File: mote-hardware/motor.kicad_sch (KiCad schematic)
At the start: 16 parts, among them J7 JST_PH_B6B, J8 JST_PH_B6B, U5 DRV8833PW

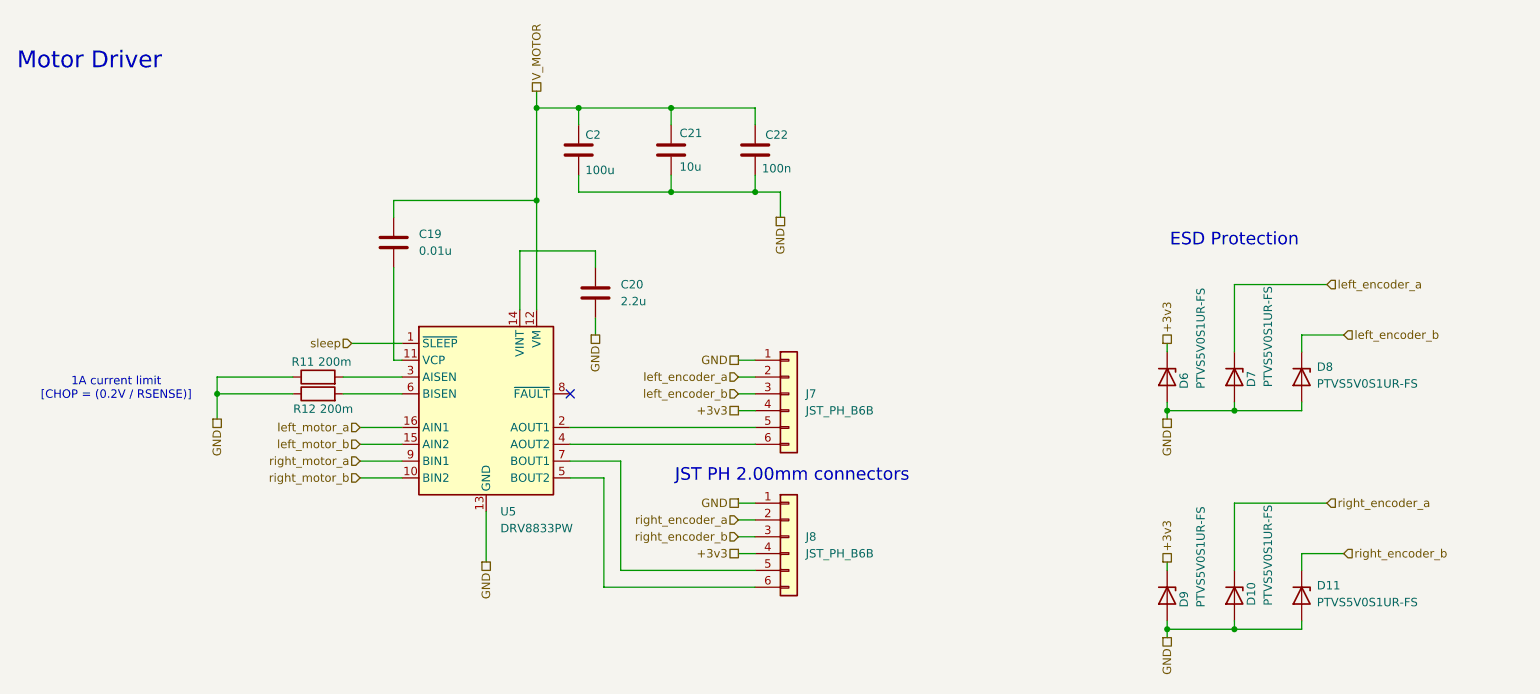
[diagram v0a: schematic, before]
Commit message: mote-hardware v0.2.0 (#63)
Improvements to the pcb design for rev v0.2.0
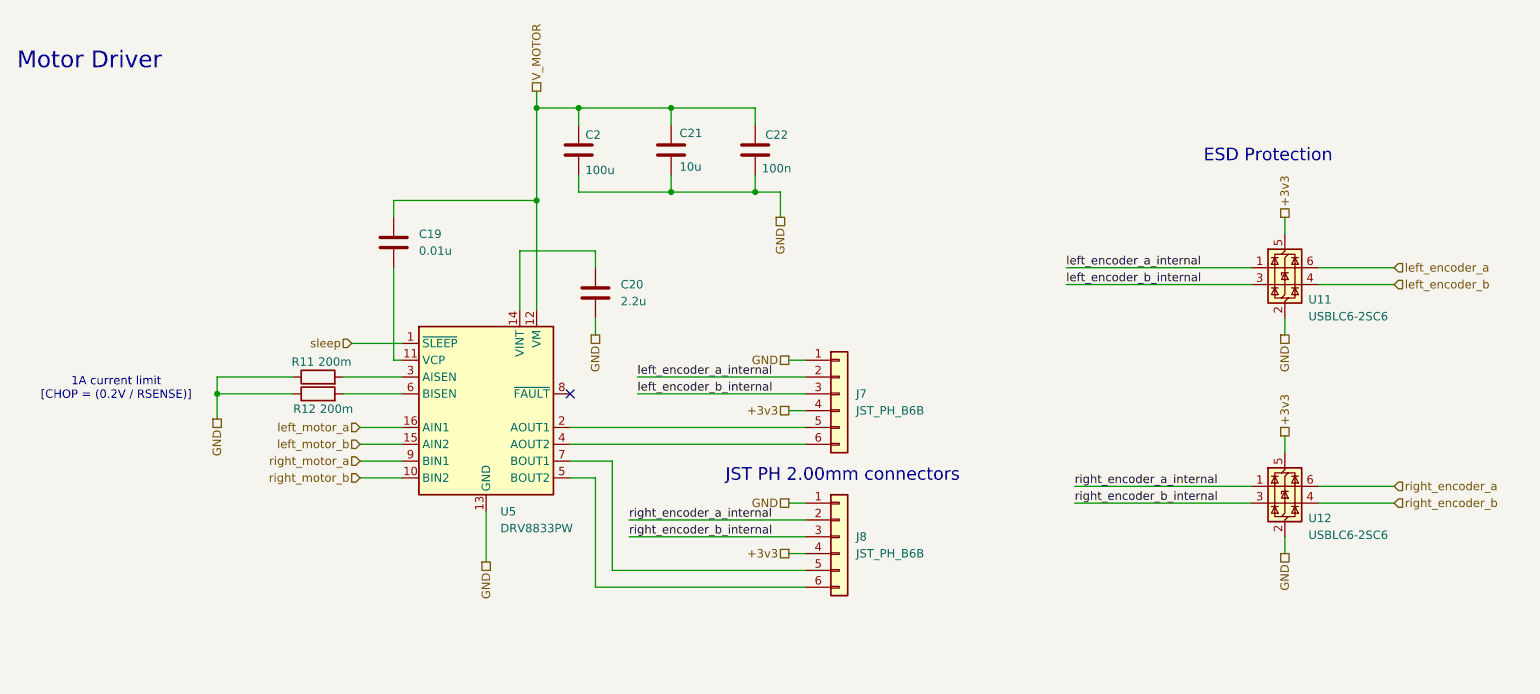
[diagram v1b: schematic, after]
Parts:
- removed D10, D11, D6, D7, D8, D9: PTVS5V0S1UR-FS, Diode_SMD:D_SOD-123, symbol Diode:PTVS5V0Z1USK
- added U11, U12: USBLC6-2SC6, Package_TO_SOT_SMD:SOT-23-6, symbol Power_Protection:USBLC6-2SC6
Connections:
- net +3v3: now also U11.5 (VBUS), U12.5 (VBUS)
- net GND: now also U11.2 (GND), U12.2 (GND)
- net left_encoder_a: now also U11.6 (I/O1); no longer J7.2 (Pin_2)
- net left_encoder_b: now also U11.4 (I/O2); no longer J7.3 (Pin_3)
- net right_encoder_a: now also U12.6 (I/O1); no longer J8.2 (Pin_2)
- net right_encoder_b: now also U12.4 (I/O2); no longer J8.3 (Pin_3)
- new net left_encoder_a_internal: J7.2 (Pin_2), U11.1 (I/O1)
- new net left_encoder_b_internal: J7.3 (Pin_3), U11.3 (I/O2)
- new net right_encoder_a_internal: J8.2 (Pin_2), U12.1 (I/O1)
- new net right_encoder_b_internal: J8.3 (Pin_3), U12.3 (I/O2)
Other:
- company: github.com/empriselab/mote-core -> github.com/empriselab/mote
- moved on the sheet: J7, J8

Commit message: Update postition and rotation values for new components (#69)
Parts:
- U11, U12: JLCPCB_CORRECTION 0; 0; 0 -> 0; 0; -90
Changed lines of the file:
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@@
 			)
 		)
-		(property "JLCPCB_CORRECTION" "0; 0; 0"
+		(property "JLCPCB_CORRECTION" "0; 0; -90"
 			(at 232.41 82.55 0)
 			(effects
@@
 			)
 		)
-		(property "JLCPCB_CORRECTION" "0; 0; 0"
+		(property "JLCPCB_CORRECTION" "0; 0; -90"
 			(at 232.41 115.57 0)
 			(effects
